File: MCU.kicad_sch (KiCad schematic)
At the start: 17 parts, among them U3 STM32L476RGTx, Y1 Crystal

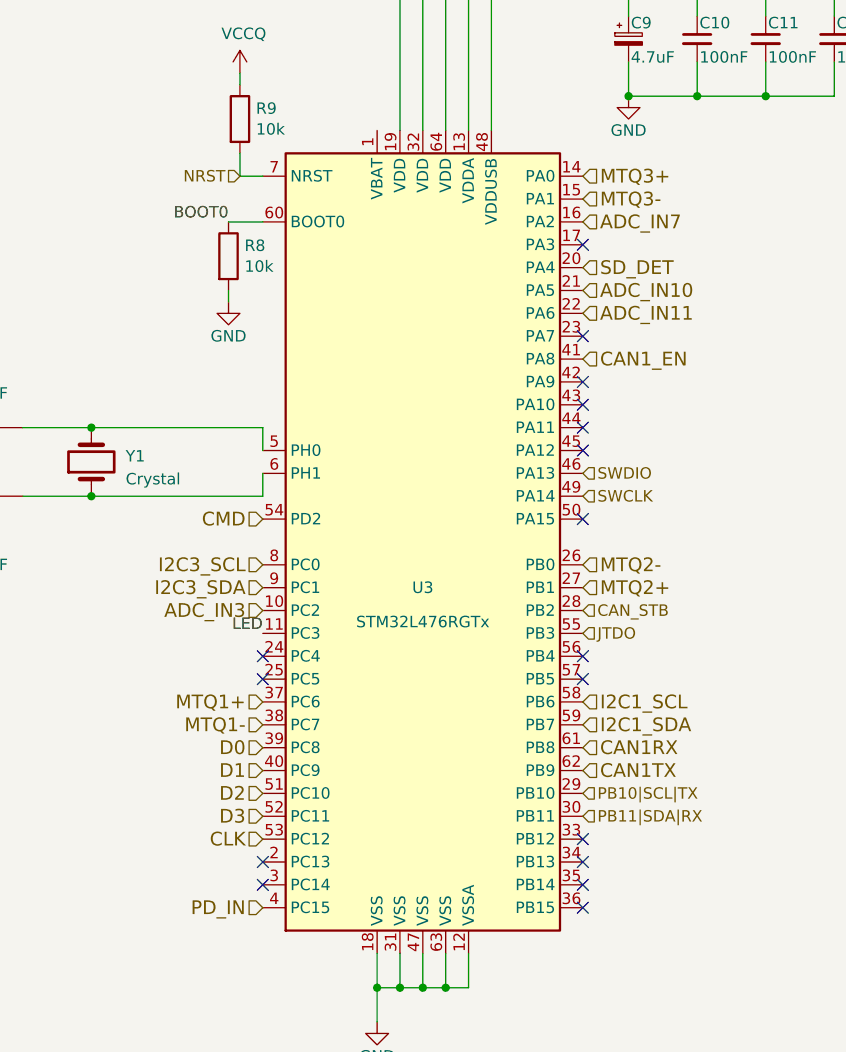
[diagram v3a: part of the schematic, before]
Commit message: Create PCB layout and routing
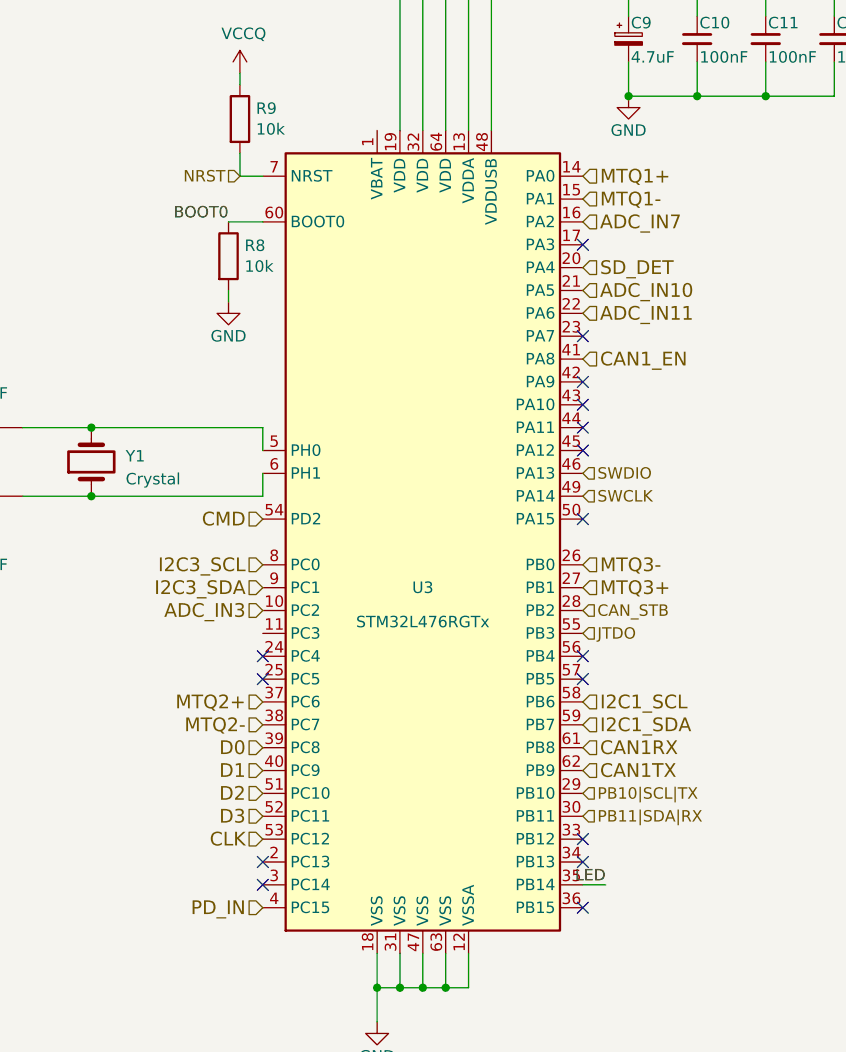
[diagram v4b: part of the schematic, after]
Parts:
- C5, C6: footprint (none) -> Library1:CAPC0603X33N
- R8, R9: footprint Resistor_SMD:R_0603_1608Metric_Pad1.05x0.95mm_HandSolder -> Resistor_SMD:R_0603_1608Metric
- Y1: footprint Crystal:Crystal_SMD_HC49-SD -> Crystal:Crystal_SMD_MicroCrystal_CC7V-T1A-2Pin_3.2x1.5mm
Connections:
- net LED: now also U3.35 (PB14); no longer U3.11 (PC3)
- net MTQ1+: now also U3.14 (PA0); no longer U3.37 (PC6)
- net MTQ1-: now also U3.15 (PA1); no longer U3.38 (PC7)
- net MTQ2+: now also U3.37 (PC6); no longer U3.27 (PB1)
- net MTQ2-: now also U3.38 (PC7); no longer U3.26 (PB0)
- net MTQ3+: now also U3.27 (PB1); no longer U3.14 (PA0)
- net MTQ3-: now also U3.26 (PB0); no longer U3.15 (PA1)
- no-connect marks 17 -> 16
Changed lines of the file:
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@@
   )
   (no_connect (at 224.79 143.51))
-  (no_connect (at 224.79 168.91))
   (no_connect (at 189.23 146.05))
   (no_connect (at 224.79 146.05))
@@
     (stroke (width 0) (type default))
   )
+  (wire (pts (xy 227.33 168.91) (xy 224.79 168.91))
+    (stroke (width 0) (type default))
+  )
   (wire (pts (xy 212.09 180.34) (xy 212.09 176.53))
     (stroke (width 0) (type default))
@@
     (effects (font (size 1.27 1.27)) (justify left bottom))
   )
-  (label "LED" (at 189.23 140.97 180) (fields_autoplaced)
-    (effects (font (size 1.27 1.27)) (justify right bottom))
-  )
   (label "LED" (at 270.51 127 180) (fields_autoplaced)
     (effects (font (size 1.27 1.27)) (justify right bottom))
   )
+  (label "LED" (at 227.33 168.91 180) (fields_autoplaced)
+    (effects (font (size 1.27 1.27)) (justify right bottom))
+  )
   (label "BOOT0" (at 185.42 95.25 180) (fields_autoplaced)
     (effects (font (size 1.27 1.27)) (justify right bottom))
   )
-  (hierarchical_label "MTQ1+" (shape input) (at 189.23 148.59 180) (fields_autoplaced)
+  (hierarchical_label "MTQ2+" (shape input) (at 189.23 148.59 180) (fields_autoplaced)
     (effects (font (size 1.524 1.524)) (justify right))
   )
@@
     (effects (font (size 1.524 1.524)) (justify right))
   )
-  (hierarchical_label "MTQ3+" (shape input) (at 224.79 90.17 0) (fields_autoplaced)
+  (hierarchical_label "MTQ1+" (shape input) (at 224.79 90.17 0) (fields_autoplaced)
     (effects (font (size 1.524 1.524)) (justify left))
   )
@@
     (effects (font (size 1.524 1.524)) (justify left))
   )
-  (hierarchical_label "MTQ2+" (shape input) (at 224.79 135.89 0) (fields_autoplaced)
-    (effects (font (size 1.524 1.524)) (justify left))
-  )
-  (hierarchical_label "MTQ2-" (shape input) (at 224.79 133.35 0) (fields_autoplaced)
-    (effects (font (size 1.524 1.524)) (justify left))
-  )
-  (hierarchical_label "MTQ3-" (shape input) (at 224.79 92.71 0) (fields_autoplaced)
+  (hierarchical_label "MTQ3+" (shape input) (at 224.79 135.89 0) (fields_autoplaced)
+    (effects (font (size 1.524 1.524)) (justify left))
+  )
+  (hierarchical_label "MTQ3-" (shape input) (at 224.79 133.35 0) (fields_autoplaced)
+    (effects (font (size 1.524 1.524)) (justify left))
+  )
+  (hierarchical_label "MTQ1-" (shape input) (at 224.79 92.71 0) (fields_autoplaced)
     (effects (font (size 1.524 1.524)) (justify left))
   )
@@
     (effects (font (size 1.27 1.27)) (justify left))
   )
-  (hierarchical_label "MTQ1-" (shape input) (at 189.23 151.13 180) (fields_autoplaced)
+  (hierarchical_label "MTQ2-" (shape input) (at 189.23 151.13 180) (fields_autoplaced)
     (effects (font (size 1.524 1.524)) (justify right))
   )
@@
       (effects (font (size 1.27 1.27)))
     )
-    (property "Footprint" "" (at 162.56 117.1448 0)
+    (property "Footprint" "Library1:CAPC0603X33N" (at 162.56 117.1448 0)
       (effects (font (size 1.27 1.27)) hide)
     )
@@
       (effects (font (size 1.27 1.27)) (justify right))
     )
-    (property "Footprint" "Crystal:Crystal_SMD_HC49-SD" (at 170.18 121.92 0)
+    (property "Footprint" "Crystal:Crystal_SMD_MicroCrystal_CC7V-T1A-2Pin_3.2x1.5mm" (at 170.18 121.92 0)
       (effects (font (size 1.27 1.27)) hide)
     )
@@
       (effects (font (size 1.27 1.27)))
     )
-    (property "Footprint" "" (at 162.56 124.7648 0)
+    (property "Footprint" "Library1:CAPC0603X33N" (at 162.56 124.7648 0)
       (effects (font (size 1.27 1.27)) hide)
     )
@@
       (effects (font (size 1.27 1.27)) (justify left))
     )
-    (property "Footprint" "Resistor_SMD:R_0603_1608Metric_Pad1.05x0.95mm_HandSolder" (at 184.912 83.82 90)
+    (property "Footprint" "Resistor_SMD:R_0603_1608Metric" (at 184.912 83.82 90)
       (effects (font (size 1.27 1.27)) hide)
     )
@@
       (effects (font (size 1.27 1.27)) (justify left))
     )
-    (property "Footprint" "Resistor_SMD:R_0603_1608Metric_Pad1.05x0.95mm_HandSolder" (at 183.642 99.06 90)
-      (effects (font (size 1.27 1.27)) hide)
-    )
+    (property "Footprint" "Resistor_SMD:R_0603_1608Metric" (at 183.642 99.06 90)
+      (effects (font (size 1.27 1.27)) hide)
+    )

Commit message: Fix some issues
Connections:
- net +3V3 renamed +3.3VP
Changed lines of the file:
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@@
-    )
-  )
-  (symbol (lib_id "power:+3.3V") (at 119.38 160.02 90) (unit 1)
-    (in_bom yes) (on_board yes) (dnp no)
-    (property "Reference" "#PWR024" (at 123.19 160.02 0)
-      (effects (font (size 1.27 1.27)) hide)
-    )
-    (property "Value" "+3.3V" (at 116.1288 159.639 90)
-      (effects (font (size 1.27 1.27)) (justify left))
-    )
-    (property "Footprint" "" (at 119.38 160.02 0)
-      (effects (font (size 1.27 1.27)) hide)
-    )
-    (property "Datasheet" "" (at 119.38 160.02 0)
-      (effects (font (size 1.27 1.27)) hide)
-    )
-    (pin "1")
-    (instances
-      (project "NEW_PCB_ADCS"
-        (path "/42c40d7d-71af-4ce9-bac9-d638f259c957/00000000-0000-0000-0000-00005a285dd1"
-          (reference "#PWR024") (unit 1)
-        )
-      )
-      (project "pq9ish-main-hw2"
-        (path "/619b49ed-1bcd-4c84-8c0f-98372f01728f/00000000-0000-0000-0000-00005a285dd1"
-          (reference "#PWR0122") (unit 1)
-        )
-      )
     )
   )
@@
     )
   )
-  (symbol (lib_name "GND_2") (lib_id "power:GND") (at 295.91 142.24 0) (unit 1)
+  (symbol (lib_id "power:GND") (at 295.91 142.24 0) (unit 1)
     (in_bom yes) (on_board yes) (dnp no) (fields_autoplaced)
     (property "Reference" "#PWR036" (at 295.91 148.59 0)
@@
     )
   )
-  (symbol (lib_name "GND_2") (lib_id "power:GND") (at 295.91 127 0) (unit 1)
+  (symbol (lib_id "power:GND") (at 295.91 127 0) (unit 1)
     (in_bom yes) (on_board yes) (dnp no)
     (property "Reference" "#PWR035" (at 295.91 133.35 0)
@@
     )
   )
-  (symbol (lib_name "GND_1") (lib_id "power:GND") (at 147.32 121.92 0) (unit 1)
+  (symbol (lib_id "power:GND") (at 147.32 121.92 0) (unit 1)
     (in_bom yes) (on_board yes) (dnp no) (fields_autoplaced)
     (property "Reference" "#PWR026" (at 147.32 128.27 0)
@@
         )
       )
+    )
+  )
+  (symbol (lib_id "power:+3.3VP") (at 119.38 160.02 90) (unit 1)
+    (in_bom yes) (on_board yes) (dnp no) (fields_autoplaced)
+    (property "Reference" "#PWR060" (at 120.65 156.21 0)
+      (effects (font (size 1.27 1.27)) hide)
+    )
+    (property "Value" "+3.3VP" (at 115.57 160.655 90)
+      (effects (font (size 1.27 1.27)) (justify left))
+    )
+    (property "Footprint" "" (at 119.38 160.02 0)
+      (effects (font (size 1.27 1.27)) hide)
+    )
+    (property "Datasheet" "" (at 119.38 160.02 0)
+      (effects (font (size 1.27 1.27)) hide)
+    )
+    (pin "1")
+    (instances
+      (project "NEW_PCB_ADCS"
+        (path "/42c40d7d-71af-4ce9-bac9-d638f259c957/00000000-0000-0000-0000-00005a289551"
+          (reference "#PWR060") (unit 1)
+        )
+        (path "/42c40d7d-71af-4ce9-bac9-d638f259c957/00000000-0000-0000-0000-00005a285dd1"
+          (reference "#PWR024") (unit 1)
+        )
+      )

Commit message: Add silk screen
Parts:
- C5, C6: footprint Library1:CAPC0603X33N -> Capacitor_SMD:C_0603_1608Metric
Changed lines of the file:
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@@
       (effects (font (size 1.27 1.27)))
     )
-    (property "Footprint" "Library1:CAPC0603X33N" (at 162.56 117.1448 0)
+    (property "Footprint" "Capacitor_SMD:C_0603_1608Metric" (at 162.56 117.1448 0)
       (effects (font (size 1.27 1.27)) hide)
     )
@@
       (effects (font (size 1.27 1.27)))
     )
-    (property "Footprint" "Library1:CAPC0603X33N" (at 162.56 124.7648 0)
-      (effects (font (size 1.27 1.27)) hide)
-    )
+    (property "Footprint" "Capacitor_SMD:C_0603_1608Metric" (at 162.56 124.7648 0)
+      (effects (font (size 1.27 1.27)) hide)
+    )

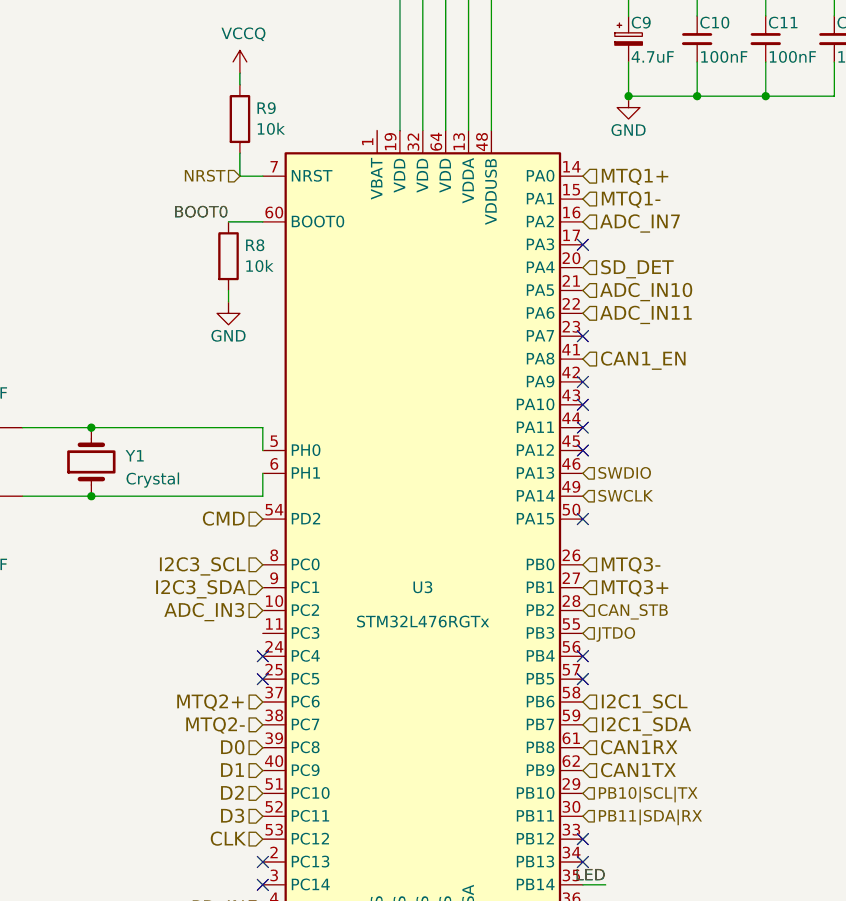
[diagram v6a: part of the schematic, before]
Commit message: Use pogo pins; move diode to back
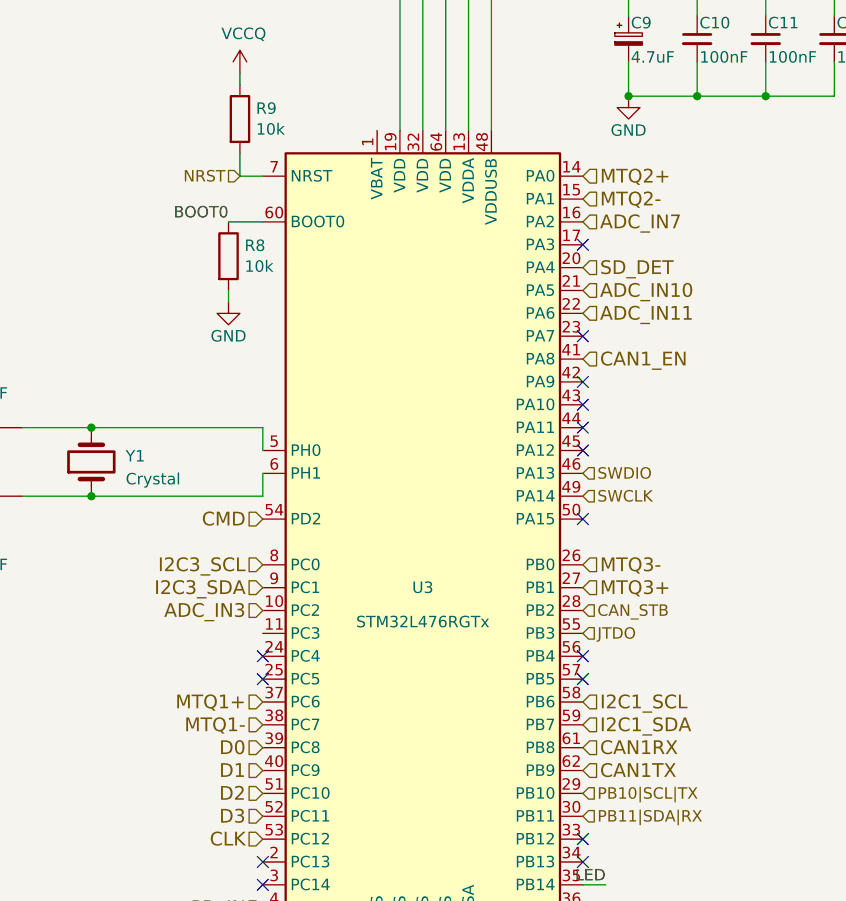
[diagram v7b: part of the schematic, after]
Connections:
- net MTQ1+: now also U3.37 (PC6); no longer U3.14 (PA0)
- net MTQ1-: now also U3.38 (PC7); no longer U3.15 (PA1)
- net MTQ2+: now also U3.14 (PA0); no longer U3.37 (PC6)
- net MTQ2-: now also U3.15 (PA1); no longer U3.38 (PC7)
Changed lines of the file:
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@@
     (effects (font (size 1.27 1.27)) (justify right bottom))
   )
-  (hierarchical_label "MTQ2+" (shape input) (at 189.23 148.59 180) (fields_autoplaced)
+  (hierarchical_label "MTQ1+" (shape input) (at 189.23 148.59 180) (fields_autoplaced)
     (effects (font (size 1.524 1.524)) (justify right))
   )
@@
     (effects (font (size 1.524 1.524)) (justify right))
   )
-  (hierarchical_label "MTQ1+" (shape input) (at 224.79 90.17 0) (fields_autoplaced)
+  (hierarchical_label "MTQ2+" (shape input) (at 224.79 90.17 0) (fields_autoplaced)
     (effects (font (size 1.524 1.524)) (justify left))
   )
@@
     (effects (font (size 1.524 1.524)) (justify left))
   )
-  (hierarchical_label "MTQ1-" (shape input) (at 224.79 92.71 0) (fields_autoplaced)
+  (hierarchical_label "MTQ2-" (shape input) (at 224.79 92.71 0) (fields_autoplaced)
     (effects (font (size 1.524 1.524)) (justify left))
   )
@@
     (effects (font (size 1.27 1.27)) (justify left))
   )
-  (hierarchical_label "MTQ2-" (shape input) (at 189.23 151.13 180) (fields_autoplaced)
+  (hierarchical_label "MTQ1-" (shape input) (at 189.23 151.13 180) (fields_autoplaced)
     (effects (font (size 1.524 1.524)) (justify right))
   )

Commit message: Update wrong MPNs
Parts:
- Y1: footprint Crystal:Crystal_SMD_MicroCrystal_CC7V-T1A-2Pin_3.2x1.5mm -> Crystal:Crystal_SMD_ECS_CSM3X-2Pin_7.6x4.1mm
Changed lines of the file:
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@@
       (effects (font (size 1.27 1.27)) (justify right))
     )
-    (property "Footprint" "Crystal:Crystal_SMD_MicroCrystal_CC7V-T1A-2Pin_3.2x1.5mm" (at 170.18 121.92 0)
+    (property "Footprint" "Crystal:Crystal_SMD_ECS_CSM3X-2Pin_7.6x4.1mm" (at 170.18 121.92 0)
       (effects (font (size 1.27 1.27)) hide)
     )
